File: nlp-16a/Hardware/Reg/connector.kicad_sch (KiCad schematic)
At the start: 47 parts, among them J1 Conn_02x20_Odd_Even, J2 Conn_02x20_Odd_Even, J3 Conn_02x20_Odd_Even, J4 Conn_02x20_Odd_Even, J5 Conn_02x16_Odd_Even, J6 Conn_02x16_Odd_Even, J7 Screw_Terminal_01x02, J8 Conn_02x10_Odd_Even

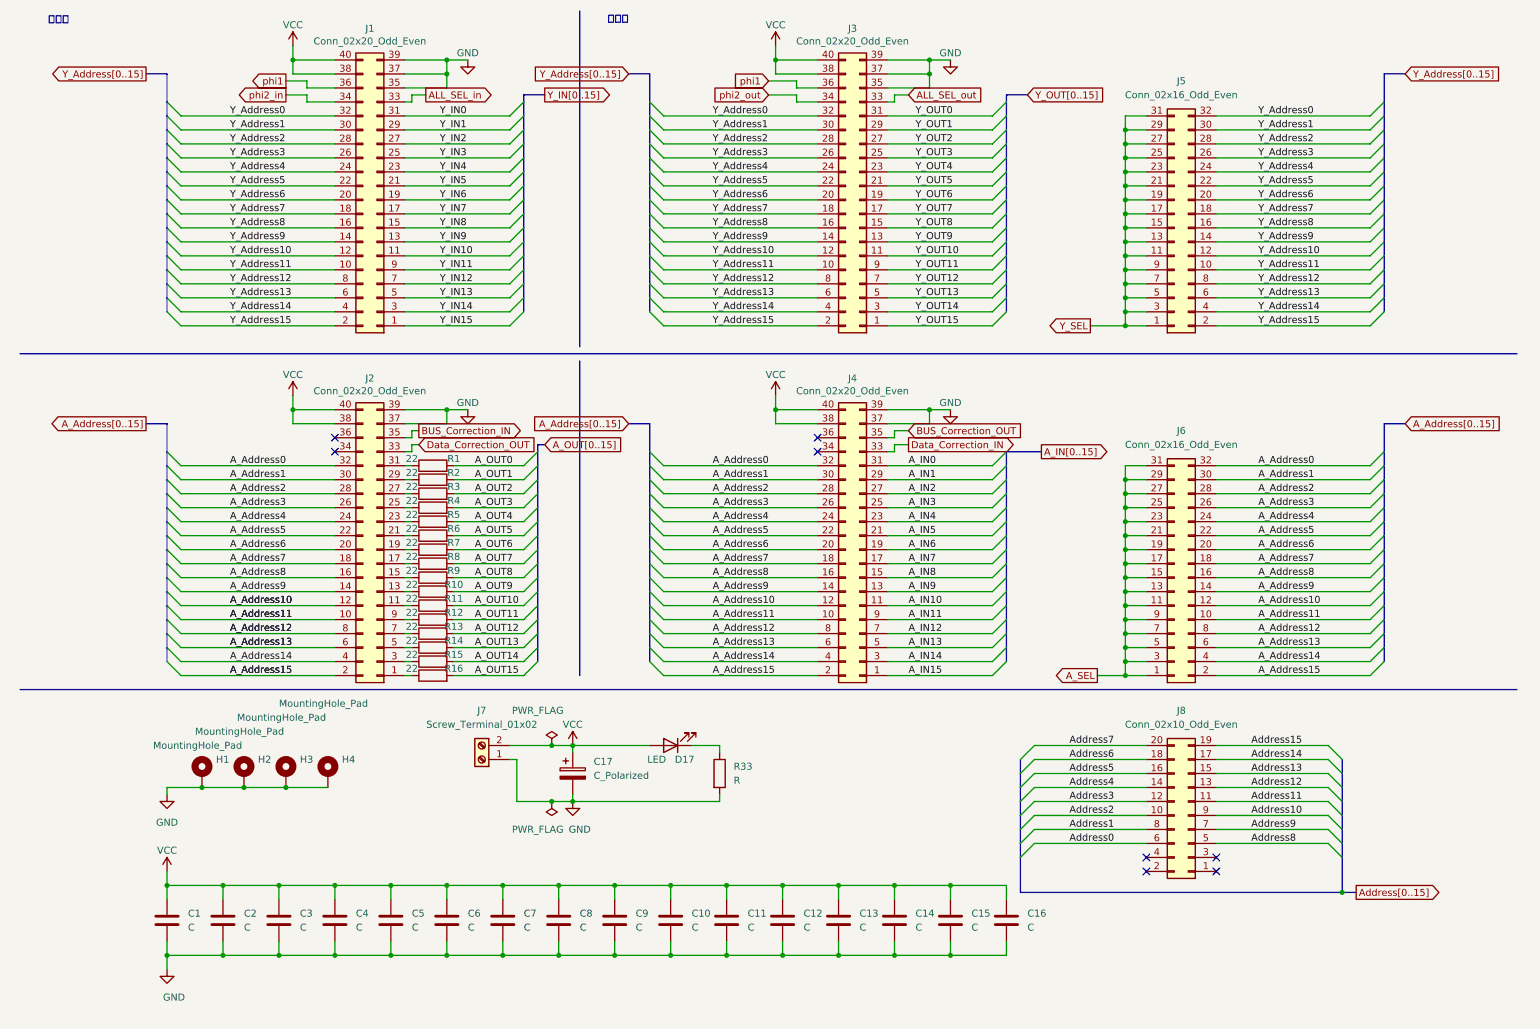
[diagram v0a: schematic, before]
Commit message: レジスタ基板だいたい完成
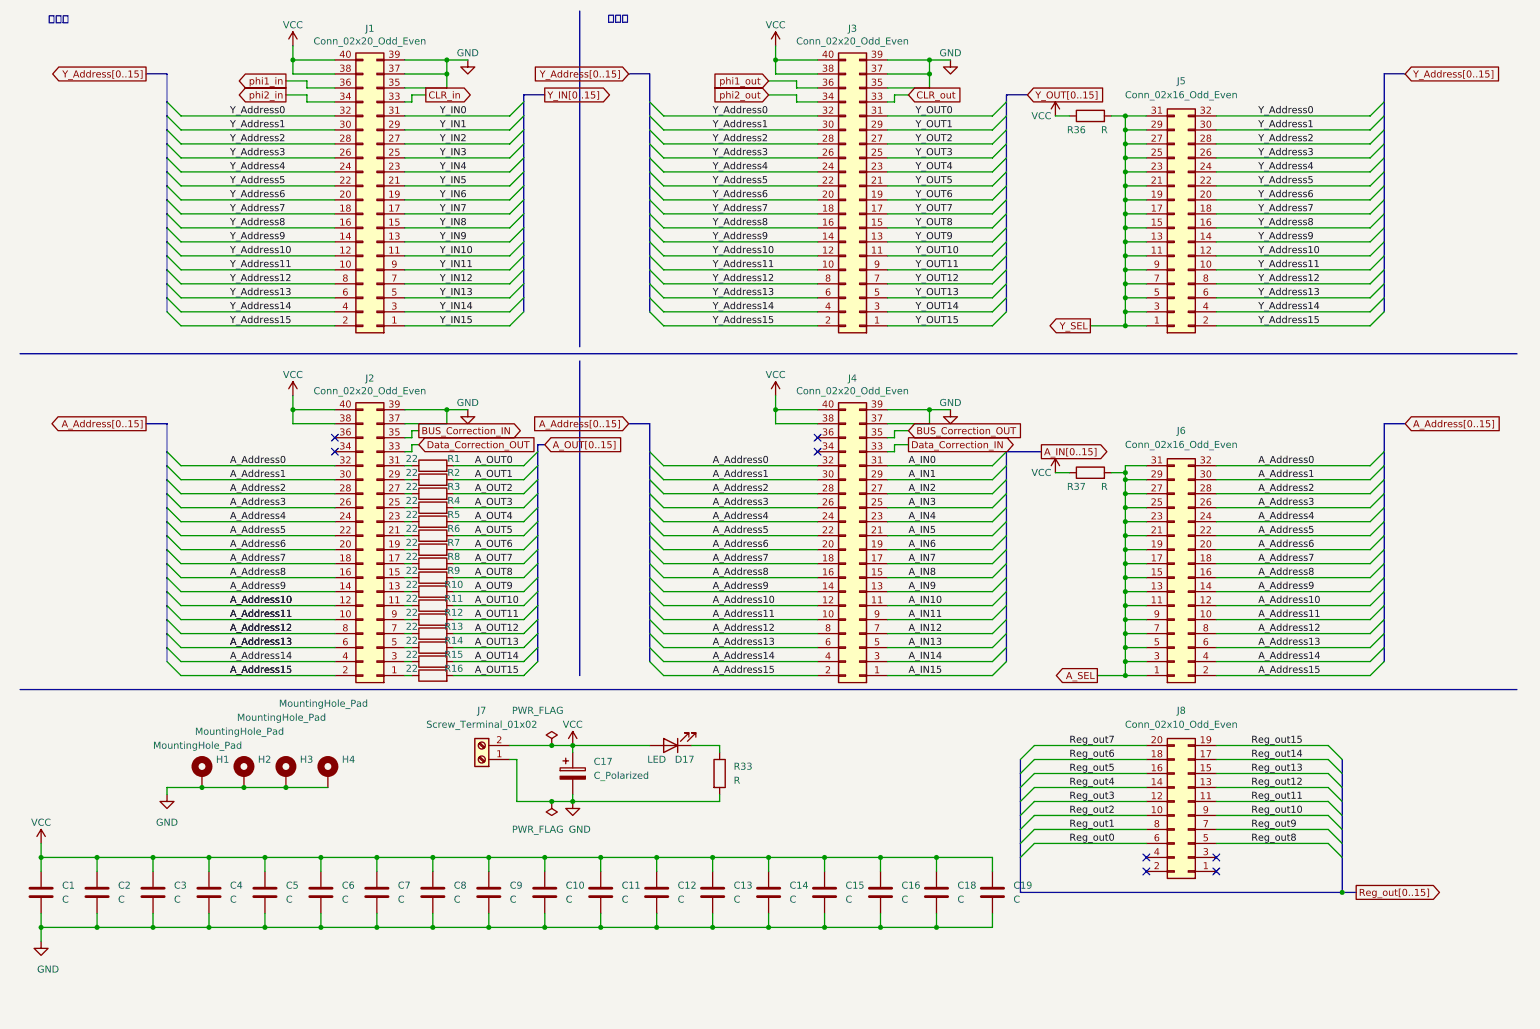
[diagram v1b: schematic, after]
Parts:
- added C18, C19: C, Capacitor_THT:C_Disc_D7.5mm_W2.5mm_P5.00mm, symbol Device:C
- added R36, R37: R, Resistor_SMD:R_0603_1608Metric_Pad0.98x0.95mm_HandSolder, symbol Device:R
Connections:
- net A_SEL: now also R37.2
- net GND: now also C18.2, C19.2
- net VCC: now also C18.1, C19.1, R36.1, R37.1
- net Y_SEL: now also R36.2
- net ALL_SEL_in renamed CLR_in
- net ALL_SEL_out renamed CLR_out
- net Address0 renamed Reg_out0
- net Address1 renamed Reg_out1
- net Address10 renamed Reg_out10
- net Address11 renamed Reg_out11
- net Address12 renamed Reg_out12
- net Address13 renamed Reg_out13
- net Address14 renamed Reg_out14
- net Address15 renamed Reg_out15
- net Address2 renamed Reg_out2
- net Address3 renamed Reg_out3
- net Address4 renamed Reg_out4
- net Address5 renamed Reg_out5
- net Address6 renamed Reg_out6
- net Address7 renamed Reg_out7
- net Address8 renamed Reg_out8
- net Address9 renamed Reg_out9
- net phi1 renamed phi1_in
- net phi1_in: no longer J3.36 (Pin_36)
- new net phi1_out: J3.36 (Pin_36)
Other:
- moved on the sheet: C1, C10, C11, C12, C13, C14, C15, C16, C2, C3, C4, C5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

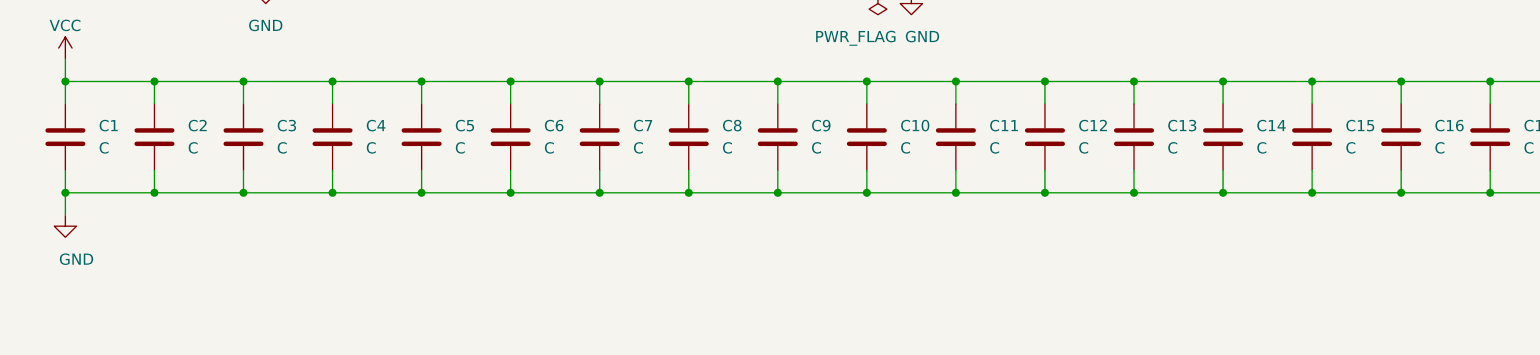
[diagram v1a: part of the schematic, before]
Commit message: テストを受けてレジスタの設計を更新
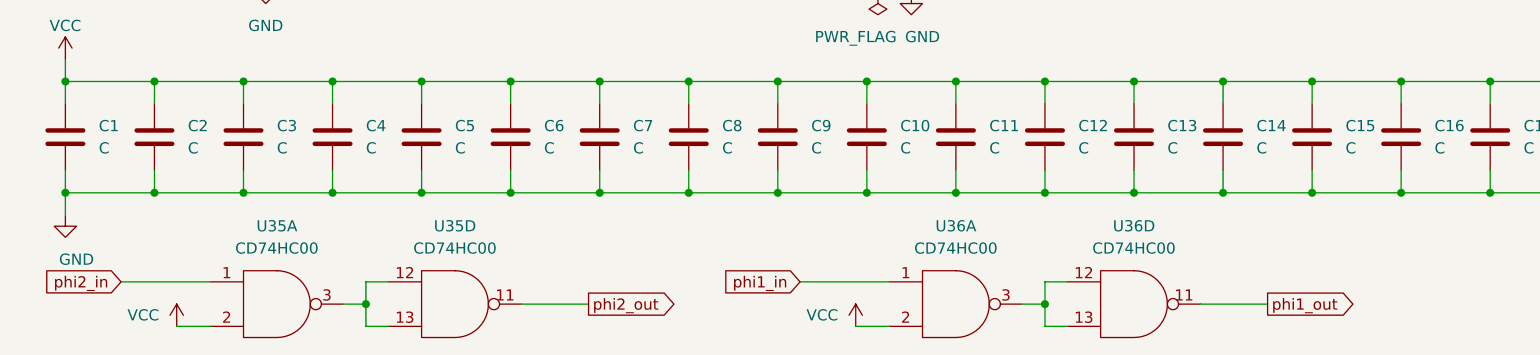
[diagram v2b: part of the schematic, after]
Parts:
- added U35, U36: CD74HC00, Package_DIP:DIP-14_W7.62mm, symbol CD74HCXX:CD74HC00
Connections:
- net GND: now also U35.7 (GND), U35.7 (GND), U36.7 (GND), U36.7 (GND)
- net VCC: now also U35.14 (VCC), U35.14 (VCC), U35.2, U36.14 (VCC), U36.14 (VCC), U36.2
- net phi1_in: now also U36.1
- net phi1_out: now also U36.11
- net phi2_in: now also U35.1
- net phi2_out: now also U35.11
- new net: U35.12, U35.13, U35.3
- new net: U36.12, U36.13, U36.3

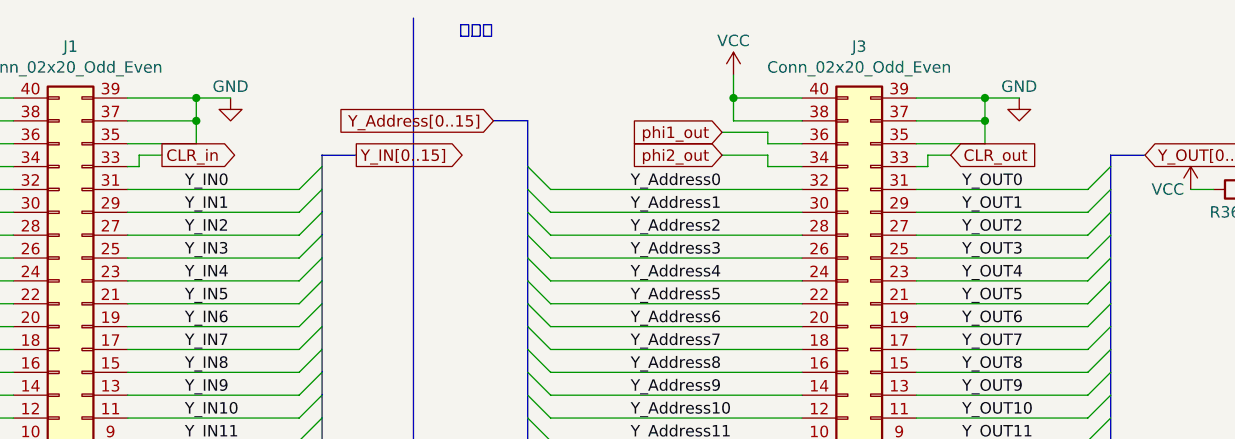
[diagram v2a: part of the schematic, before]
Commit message: レジスタクリア時の動作を修正
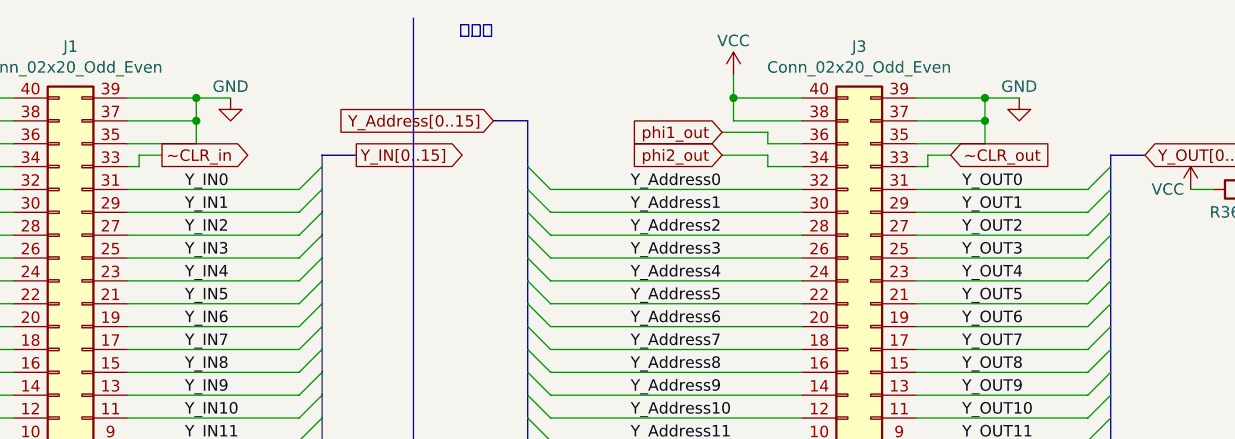
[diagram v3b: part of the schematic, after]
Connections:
- net CLR_in renamed ~CLR_in
- net CLR_out renamed ~CLR_out
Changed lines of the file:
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@@
     )
   )
-  (global_label "CLR_in" (shape output) (at 86.36 29.21 0) (fields_autoplaced)
+  (global_label "~CLR_in" (shape output) (at 86.36 29.21 0) (fields_autoplaced)
     (effects (font (size 1.27 1.27)) (justify left))
-    (property "Intersheet References" "${INTERSHEET_REFS}" (id 0) (at 95.0626 29.1306 0)
+    (property "Intersheet References" "${INTERSHEET_REFS}" (id 0) (at 95.9698 29.1306 0)
       (effects (font (size 1.27 1.27)) (justify left) hide)
     )
   )
-  (global_label "CLR_out" (shape input) (at 173.99 29.21 0) (fields_autoplaced)
+  (global_label "~CLR_out" (shape input) (at 173.99 29.21 0) (fields_autoplaced)
     (effects (font (size 1.27 1.27)) (justify left))
-    (property "Intersheet References" "${INTERSHEET_REFS}" (id 0) (at 183.9626 29.1306 0)
+    (property "Intersheet References" "${INTERSHEET_REFS}" (id 0) (at 184.8698 29.1306 0)
       (effects (font (size 1.27 1.27)) (justify left) hide)
     )

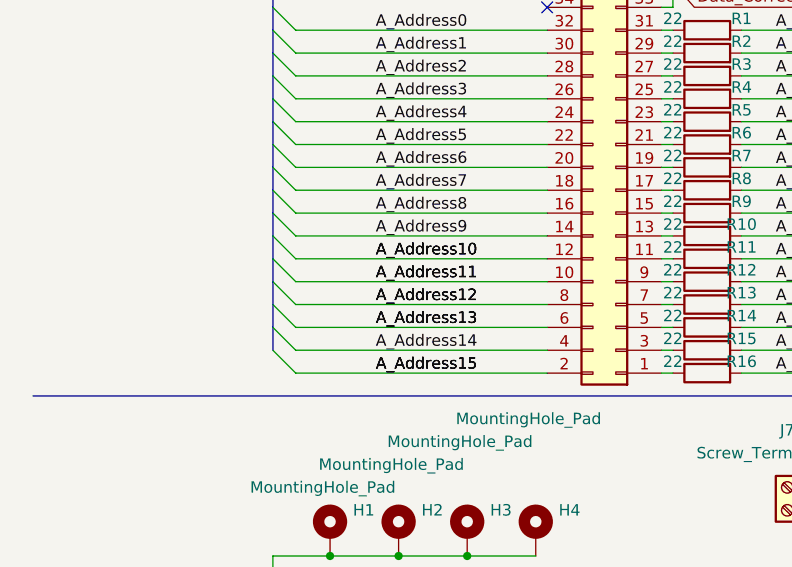
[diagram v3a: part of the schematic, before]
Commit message: v1.1全ガーバーを更新
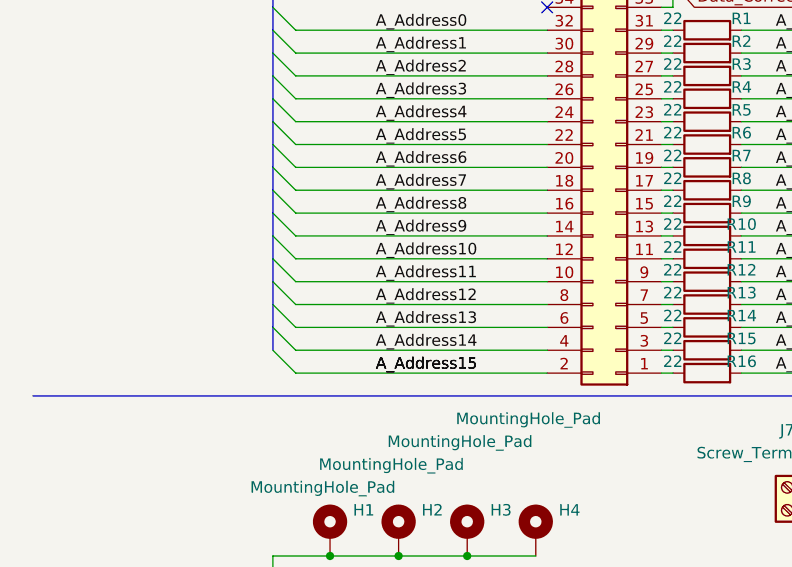
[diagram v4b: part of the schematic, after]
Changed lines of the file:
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@@
+    (stroke (width 0) (type default) (color 0 0 0 0))
+  )
+  (bus_entry (at 39.37 127) (size 2.54 2.54)
     (stroke (width 0) (type default) (color 0 0 0 0))
   )
@@
     (stroke (width 0) (type default) (color 0 0 0 0))
   )
-  (bus_entry (at 39.37 127) (size 2.54 2.54)
-    (stroke (width 0) (type default) (color 0 0 0 0))
-  )
   (bus_entry (at 39.37 132.08) (size 2.54 2.54)
     (stroke (width 0) (type default) (color 0 0 0 0))
@@
     (stroke (width 0) (type default) (color 0 0 0 0))
   )
-  (bus (pts (xy 39.37 129.54) (xy 39.37 127))
-    (stroke (width 0) (type default) (color 0 0 0 0))
-  )
   (wire (pts (xy 26.67 177.8) (xy 26.67 180.34))
     (stroke (width 0) (type default) (color 0 0 0 0))
@@
     (stroke (width 0) (type default) (color 0 0 0 0))
   )
-  (bus (pts (xy 39.37 127) (xy 39.37 124.46))
+  (bus (pts (xy 39.37 124.46) (xy 39.37 127))
     (stroke (width 0) (type default) (color 0 0 0 0))
   )
@@
     (stroke (width 0) (type default) (color 0 0 0 0))
   )
+  (bus (pts (xy 39.37 127) (xy 39.37 129.54))
+    (stroke (width 0) (type default) (color 0 0 0 0))
+  )
   (wire (pts (xy 83.82 114.3) (xy 82.55 114.3))
     (stroke (width 0) (type default) (color 0 0 0 0))
@@
     (effects (font (size 1.27 1.27)) (justify left bottom))
   )
-  (label "A_Address10" (at 50.8 121.92 0)
-    (effects (font (size 1.27 1.27)) (justify left bottom))
-  )
   (label "Y_Address1" (at 237.49 35.56 0)
     (effects (font (size 1.27 1.27)) (justify left bottom))
@@
     (effects (font (size 1.27 1.27)) (justify left bottom))
   )
-  (label "A_Address11" (at 50.8 124.46 0)
-    (effects (font (size 1.27 1.27)) (justify left bottom))
-  )
   (label "A_IN15" (at 173.99 134.62 0)
     (effects (font (size 1.27 1.27)) (justify left bottom))
@@
     (effects (font (size 1.27 1.27)) (justify left bottom))
   )
-  (label "A_Address12" (at 50.8 127 0)
-    (effects (font (size 1.27 1.27)) (justify left bottom))
-  )
   (label "A_Address0" (at 237.49 96.52 0)
     (effects (font (size 1.27 1.27)) (justify left bottom))
@@
     (effects (font (size 1.27 1.27)) (justify left bottom))
   )
-  (label "A_Address13" (at 50.8 129.54 0)
-    (effects (font (size 1.27 1.27)) (justify left bottom))
-  )
